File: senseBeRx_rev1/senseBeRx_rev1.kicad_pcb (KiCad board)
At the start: 2 copper layers, 40 x 80 mm, 35 parts, among them J1 SJ2-35863B1-SMT, J2 SJ2-35863B1-SMT, P1 CONN_02X05, Q1 TSM2301, Q2 SI2302, Q3 SI2302, Q4 SI2302, SW1 SW_DPST, U1 MDBT42Q, U2 TSSP4056, Y1 T38 Mercury

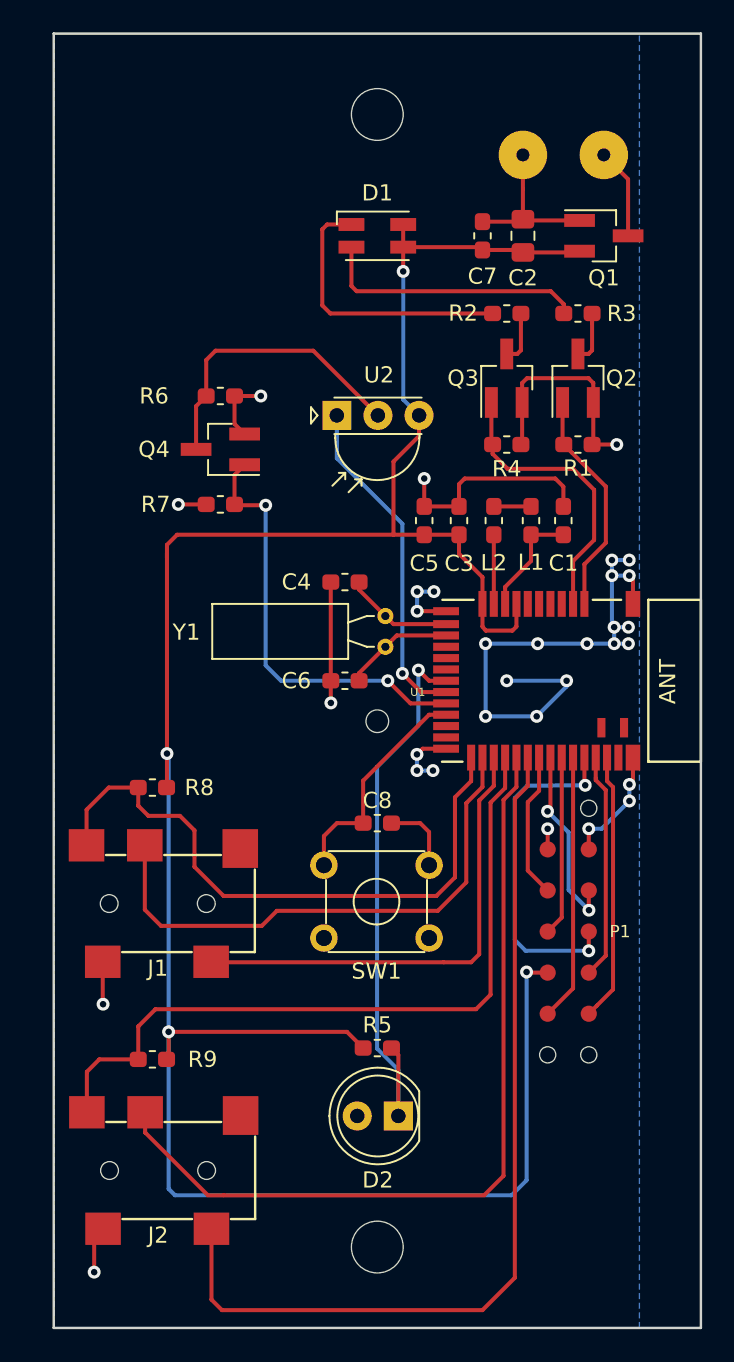
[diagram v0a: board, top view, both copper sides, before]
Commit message: Adds Appiko Logo in the Silkscreen, and Gerber files for manufacturing
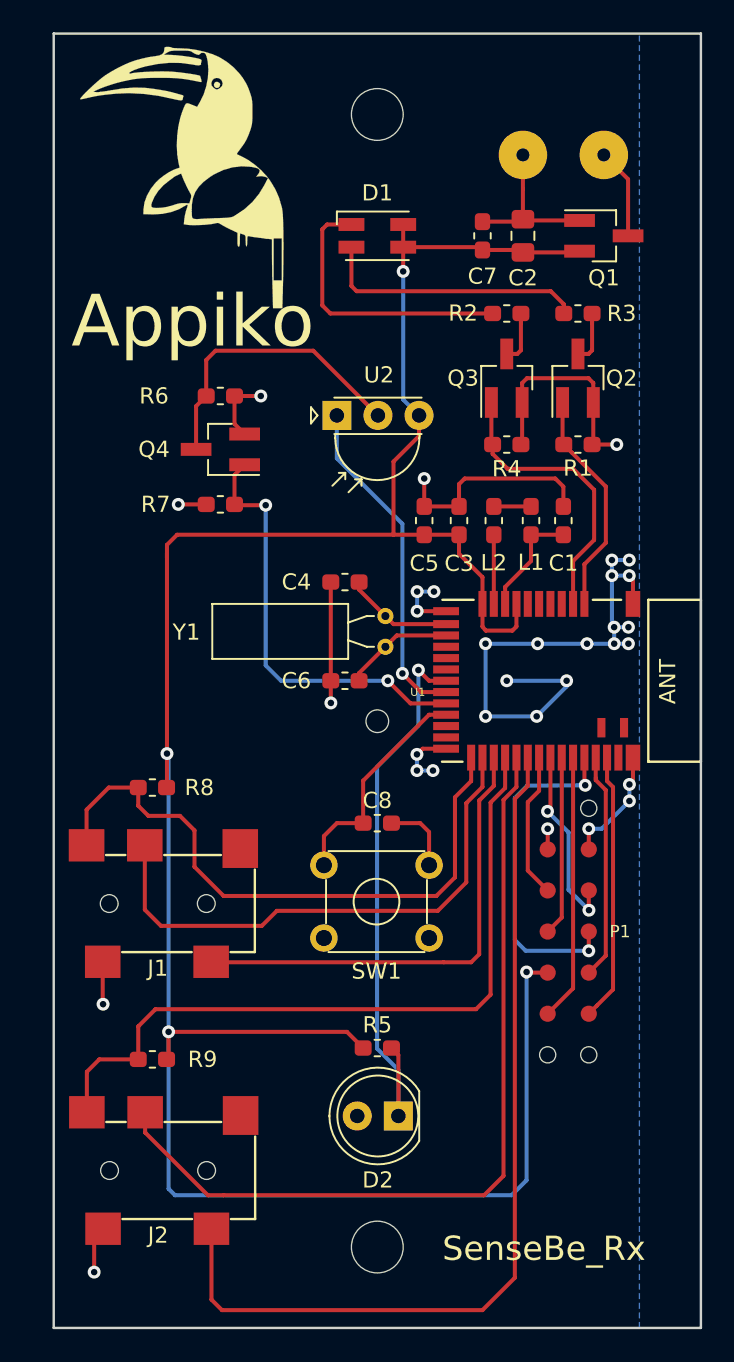
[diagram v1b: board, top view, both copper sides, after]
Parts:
- added G***: LOGO, senseBeRx_rev1_fp:LOGO, F.Cu at (107.9, 78.9)
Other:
- board text added: "SenseBe_Rx"

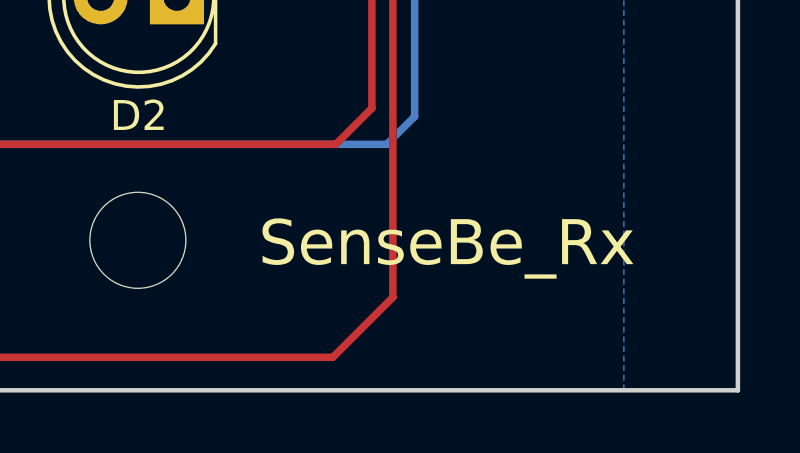
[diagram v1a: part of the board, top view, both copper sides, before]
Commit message: Add V1 label on silkscreen
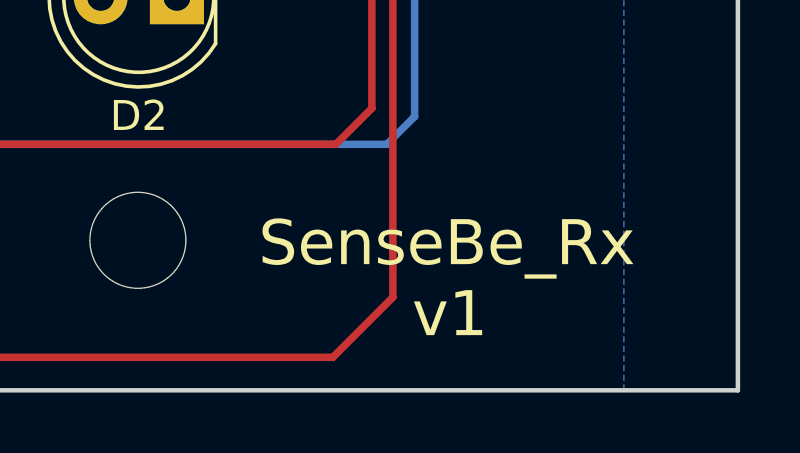
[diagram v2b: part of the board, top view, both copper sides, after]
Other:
- board text added: "v1"
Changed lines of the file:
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@@
   (general
     (thickness 1.6)
-    (drawings 9)
+    (drawings 10)
     (tracks 332)
     (zones 0)
@@
     (visible_elements FFFFFF7F)
     (pcbplotparams
-      (layerselection 0x010fc_ffffffff)
-      (usegerberextensions false)
+      (layerselection 0x010f0_ffffffff)
+      (usegerberextensions true)
       (usegerberattributes false)
       (usegerberadvancedattributes false)
@@
     )
   )
+  (gr_text v1 (at 130.4036 147.46732) (layer F.SilkS)
+    (effects (font (size 1.5 1.5) (thickness 0.3)))
+  )
   (gr_text SenseBe_Rx (at 130.3 145.1) (layer F.SilkS)
